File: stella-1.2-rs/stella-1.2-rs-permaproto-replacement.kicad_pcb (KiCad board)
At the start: 2 copper layers, 81.3 x 50.8 mm, 10 parts, among them J1 Conn_01x03, J2 Conn_01x04, U1 Triad, U2 Humidity, U3 Surface Temp, U4 Range

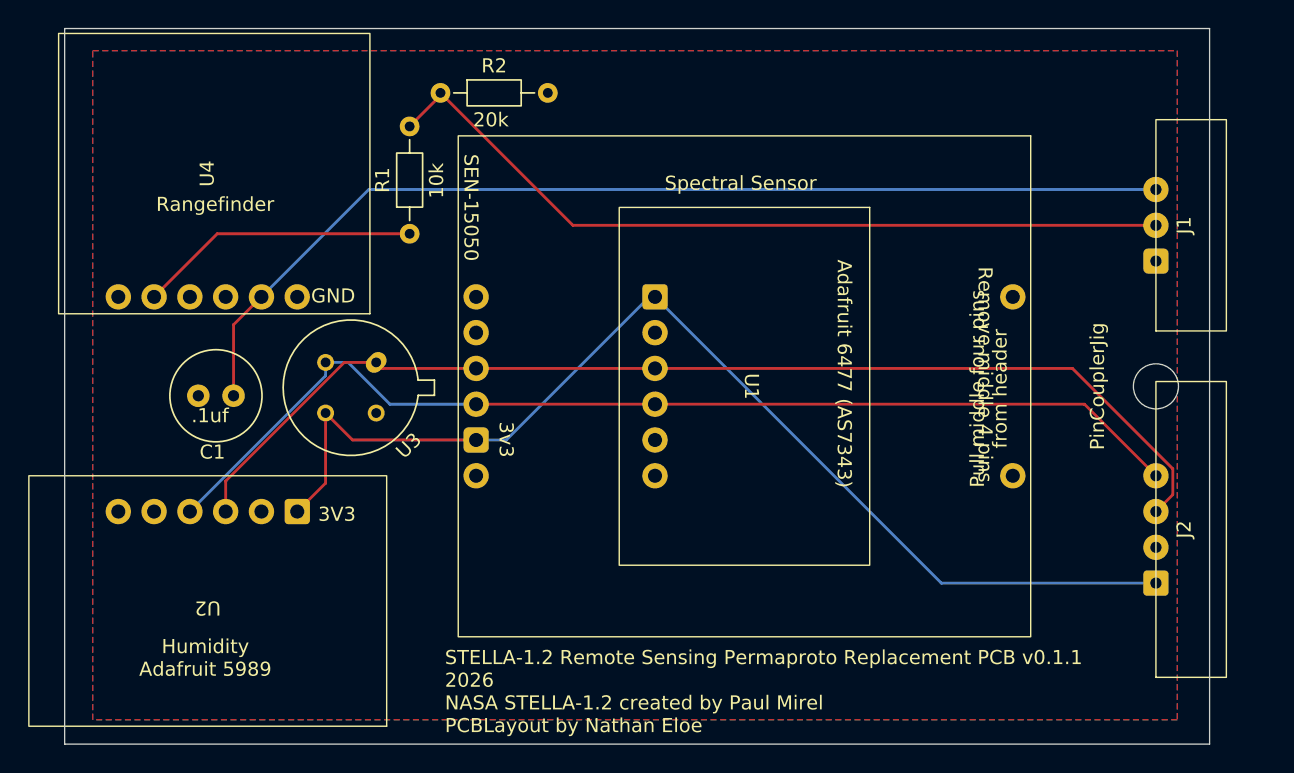
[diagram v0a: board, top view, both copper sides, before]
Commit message: Clean up silkscreen for RS PCB
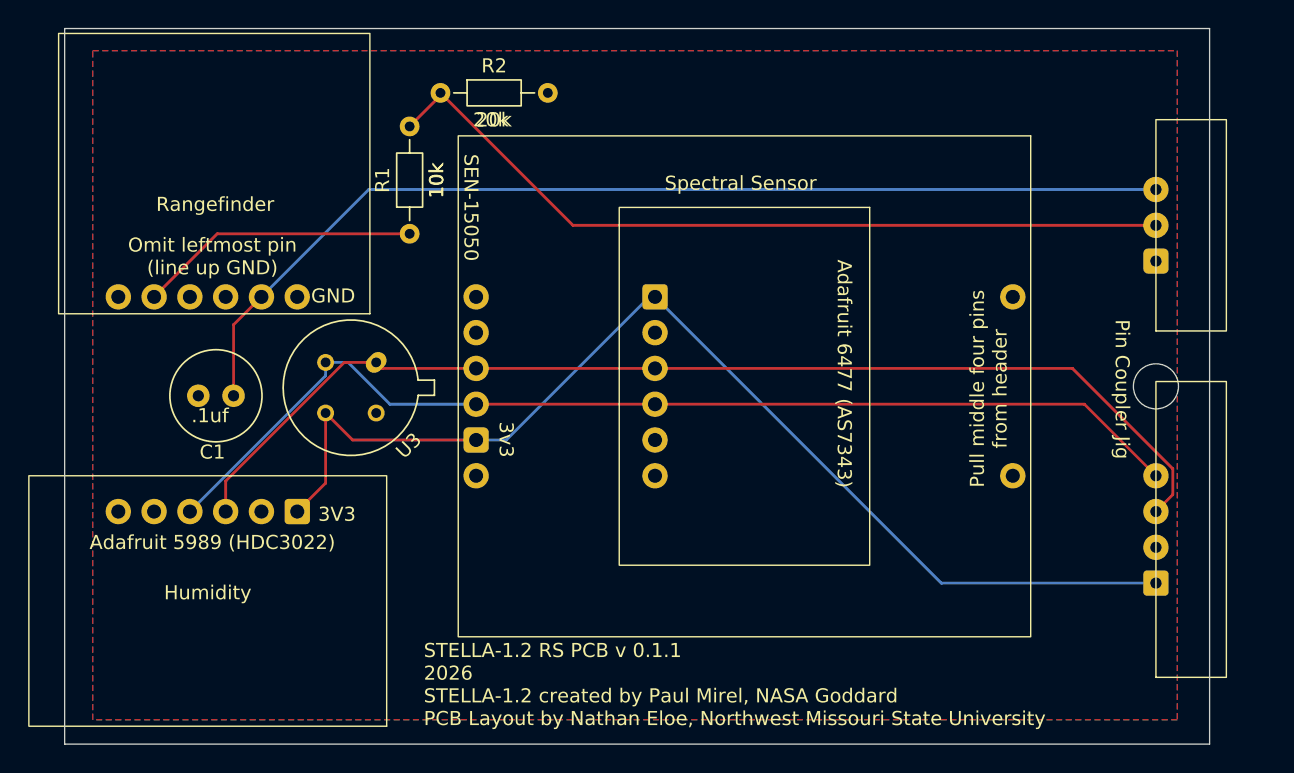
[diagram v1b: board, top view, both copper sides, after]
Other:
- board text added: "Adafruit 5989 (HDC3022)"
- board text added: "Humidity"
- board text added: "Omit leftmost pin (line up GND)"
- board text added: "Pin Coupler Jig"
- board text added: "STELLA-1.2 RS PCB v 0.1.1 2026 STELLA-1.2 created by Paul Mirel, NASA Goddard PCB Layout by Nathan Eloe, Northwest Missouri State University"
- board text removed: "Humidity Adafruit 5989"
- board text removed: "STELLA-1.2 Remote Sensing Permaproto Replacement PCB v0.1.1 2026 NASA STELLA-1.2 created by Paul Mirel PCBLayout by Nathan Eloe"
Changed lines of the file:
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@@
 			(unlocked yes)
 			(layer "F.SilkS")
+			(hide yes)
 			(effects
 				(font
@@
 			)
 		)
-		(fp_text user "Remove middle 4 pins"
-			(at -8.5 -16.5 270)
-			(unlocked yes)
-			(layer "F.SilkS")
-			(effects
-				(font
-					(size 1 1)
-					(thickness 0.1)
-				)
-				(justify left bottom)
-			)
-		)
 		(fp_text user "${REFERENCE}"
 			(at 0 2.5 270)
@@
 			(unlocked yes)
 			(layer "F.SilkS")
+			(hide yes)
 			(effects
 				(font
@@
 			(unlocked yes)
 			(layer "F.SilkS")
+			(hide yes)
 			(effects
 				(font
@@
 			(unlocked yes)
 			(layer "F.SilkS")
+			(hide yes)
 			(effects
 				(font
@@
 		(property "Value" "10k"
 			(at 3.81 1.92 90)
-			(layer "F.Fab")
+			(layer "F.SilkS")
 			(effects
 				(font
@@
 			(at 0 -4.15 90)
 			(layer "F.SilkS")
+			(hide yes)
 			(effects
 				(font
@@
 		(property "Value" "20k"
 			(at 3.81 1.92 0)
-			(layer "F.Fab")
+			(layer "F.SilkS")
 			(effects
 				(font
@@
 			(unlocked yes)
 			(layer "F.SilkS")
+			(hide yes)
 			(effects
 				(font
@@
 		)
 	)
-	(gr_text "STELLA-1.2 Remote Sensing Permaproto Replacement PCB v0.1.1\n2026\nNASA STELLA-1.2 created by Paul Mirel\nPCBLayout by Nathan Eloe\n"
-		(at 107 125 0)
-		(layer "F.SilkS")
-		(effects
-			(font
-				(size 1 1)
-				(thickness 0.1)
-			)
-			(justify left bottom)
-		)
-	)
 	(gr_text "20k"
 		(at 109 82 0)
@@
 		)
 	)
-	(gr_text "Humidity\nAdafruit 5989"
-		(at 90 121 0)
+	(gr_text "Humidity"
+		(at 90.17 115.57 0)
+		(layer "F.SilkS")
+		(effects
+			(font
+				(size 1 1)
+				(thickness 0.1)
+			)
+			(justify bottom)
+		)
+	)
+	(gr_text "Omit leftmost pin\n(line up GND)"
+		(at 90.5 92.5 0)
+		(layer "F.SilkS")
+		(effects
+			(font
+				(size 1 1)
+				(thickness 0.1)
+			)
+			(justify bottom)
+		)
+	)
+	(gr_text "Adafruit 5989 (HDC3022)"
+		(at 90.5 112 0)
 		(layer "F.SilkS")
 		(effects
@@
 		)
 	)
+	(gr_text "Pin Coupler Jig"
+		(at 154.5 100.54 270)
+		(layer "F.SilkS")
+		(effects
+			(font
+				(size 1 1)
+				(thickness 0.1)
+			)
+			(justify bottom)
+		)
+	)
+	(gr_text "STELLA-1.2 RS PCB v 0.1.1\n2026\nSTELLA-1.2 created by Paul Mirel, NASA Goddard\nPCB Layout by Nathan Eloe, Northwest Missouri State University"
+		(at 105.5 124.5 0)
+		(layer "F.SilkS")
+		(effects
+			(font
+				(size 1 1)
+				(thickness 0.15)
+			)
+			(justify left bottom)
+		)
+	)

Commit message: Tighten attribution to 3 lines
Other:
- board text added: "STELLA-1.2 RS PCB v 0.1.1, 2026 STELLA-1.2 created by Paul Mirel, NASA Goddard PCB Layout by Nathan Eloe, Northwest Missouri State University"
- board text added: "Surface Temp"
- board text removed: "STELLA-1.2 RS PCB v 0.1.1 2026 STELLA-1.2 created by Paul Mirel, NASA Goddard PCB Layout by Nathan Eloe, Northwest Missouri State University"
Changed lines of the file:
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@@
 		(tags "TO-39-4")
 		(property "Reference" "U3"
-			(at 0 -5.809999 225)
-			(layer "F.SilkS")
+			(at 0 -5.809999 45)
+			(layer "F.SilkS")
+			(hide yes)
 			(effects
 				(font
@@
 		)
 		(property "Value" "Surface Temp"
-			(at 0 5.809999 225)
+			(at 0 5.809999 45)
 			(layer "F.Fab")
 			(effects
@@
 		)
 		(property "Datasheet" ""
-			(at 0 0 225)
+			(at 0 0 45)
 			(layer "F.Fab")
 			(hide yes)
@@
 		)
 		(property "Description" ""
-			(at 0 0 225)
+			(at 0 0 45)
 			(layer "F.Fab")
 			(hide yes)
@@
 		)
 		(property "KiLib_Generator" "package/TO_SOT/THT"
-			(at 0 0 225)
+			(at 0 0 45)
 			(layer "F.SilkS")
 			(hide yes)
@@
 		)
 		(fp_text user "${REFERENCE}"
-			(at 0 -5.809999 225)
+			(at 0 -5.809999 45)
 			(layer "F.Fab")
 			(effects
@@
 		(layer "Edge.Cuts")
 	)
+	(gr_text "Surface Temp"
+		(at 100.5 101 0)
+		(layer "F.SilkS")
+		(effects
+			(font
+				(size 0.8 0.8)
+				(thickness 0.1)
+			)
+			(justify bottom)
+		)
+	)
 	(gr_text "Rangefinder"
 		(at 86.5 88 0)
@@
 		)
 	)
-	(gr_text "STELLA-1.2 RS PCB v 0.1.1\n2026\nSTELLA-1.2 created by Paul Mirel, NASA Goddard\nPCB Layout by Nathan Eloe, Northwest Missouri State University"
-		(at 105.5 124.5 0)
+	(gr_text "STELLA-1.2 RS PCB v 0.1.1, 2026\nSTELLA-1.2 created by Paul Mirel, NASA Goddard\nPCB Layout by Nathan Eloe, Northwest Missouri State University"
+		(at 105.5 123.5 0)
 		(layer "F.SilkS")
 		(effects

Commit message: Add pins for SHT4x to RS
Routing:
- net /I2C_SDA: track 76.9 -> 105.5 mm
- net /I2C_SCL: track 79.6 -> 105.7 mm
- net +3V3: track 80.2 -> 97.6 mm
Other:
- board text added: "Adafruit 4885/5776/6174 (SHT4X)"
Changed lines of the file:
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@@
+			(pintype "power_in")
+		)
+		(pad "1" thru_hole roundrect
+			(at 5.08 -6.35 180)
+			(size 1.8 1.8)
+			(drill 1)
+			(layers "*.Cu" "*.Mask")
+			(remove_unused_layers no)
+			(roundrect_rratio 0.15)
+			(net "+3V3")
+			(pinfunction "VCC_1")
 			(pintype "power_in")
 		)
@@
 			(pintype "power_in")
 		)
+		(pad "2" thru_hole circle
+			(at 0 -6.35 180)
+			(size 1.8 1.8)
+			(drill 1)
+			(layers "*.Cu" "*.Mask")
+			(remove_unused_layers no)
+			(net "GND")
+			(pinfunction "GND_2")
+			(pintype "power_in")
+		)
 		(pad "3" thru_hole circle
-			(at -1.27 6.35 180)
+			(at -2.54 -6.35 180)
 			(size 1.8 1.8)
 			(drill 1)
@@
 			(pintype "input")
 		)
+		(pad "3" thru_hole circle
+			(at -1.27 6.35 180)
+			(size 1.8 1.8)
+			(drill 1)
+			(layers "*.Cu" "*.Mask")
+			(remove_unused_layers no)
+			(net "/I2C_SCL")
+			(pinfunction "SCL_3")
+			(pintype "input")
+		)
 		(pad "4" thru_hole circle
-			(at 1.27 6.35 180)
+			(at -5.08 -6.35 180)
 			(size 1.8 1.8)
 			(drill 1)
@@
 			(pintype "output")
 		)
+		(pad "4" thru_hole circle
+			(at 1.27 6.35 180)
+			(size 1.8 1.8)
+			(drill 1)
+			(layers "*.Cu" "*.Mask")
+			(remove_unused_layers no)
+			(net "/I2C_SDA")
+			(pinfunction "SDA_4")
+			(pintype "output")
+		)
 		(pad "5" thru_hole circle
 			(at 3.81 6.35 180)
@@
 			(pinfunction "~{RES}_5")
 			(pintype "input+no_connect")
+		)
+		(pad "6" thru_hole circle
+			(at 2.54 -6.35 180)
+			(size 1.8 1.8)
+			(drill 1)
+			(layers "*.Cu" "*.Mask")
+			(remove_unused_layers no)
+			(net "unconnected-(U2-ALERT-Pad6)_1")
+			(pinfunction "ALERT_6")
+			(pintype "output+no_connect")
 		)
 		(pad "6" thru_hole circle
@@
 		)
 	)
+	(gr_text "3V3"
+		(at 80.5 122.5 0)
+		(layer "F.SilkS")
+		(effects
+			(font
+				(size 1 1)
+				(thickness 0.1)
+			)
+			(justify left bottom)
+		)
+	)
 	(gr_text "Rangefinder"
 		(at 86.5 88 0)
@@
 		)
 	)
+	(gr_text "3V3"
+		(at 120.5 93 0)
+		(layer "F.SilkS")
+		(effects
+			(font
+				(size 1 1)
+				(thickness 0.1)
+			)
+			(justify left bottom)
+		)
+	)
+	(gr_text "Adafruit 4885/5776/6174\n(SHT4X)"
+		(at 91 119.5 0)
+		(layer "F.SilkS")
+		(effects
+			(font
+				(size 1 1)
+				(thickness 0.1)
+			)
+		)
+	)
 	(gr_text "Humidity"
 		(at 90.17 115.57 0)
@@
 	)
 	(segment
+		(start 92.71 121.92)
+		(end 91.51 123.12)
+		(width 0.2)
+		(layer "F.Cu")
+		(net "/I2C_SCL")
+	)
+	(segment
 		(start 109.22 99.06)
 		(end 102.552102 99.06)
@@
 	)
 	(segment
+		(start 83.89 116.77)
+		(end 91.44 109.22)
+		(width 0.2)
+		(layer "F.Cu")
+		(net "/I2C_SCL")
+	)
+	(segment
 		(start 151.557057 99.06)
 		(end 121.92 99.06)
@@
 	)
 	(segment
+		(start 91.51 123.12)
+		(end 84.216418 123.12)
+		(width 0.2)
+		(layer "F.Cu")
+		(net "/I2C_SCL")
+	)
+	(segment
 		(start 102.552102 99.06)
 		(end 102.126051 98.633949)
@@
 	)
 	(segment
+		(start 83.89 122.793582)
+		(end 83.89 116.77)
+		(width 0.2)
+		(layer "F.Cu")
+		(net "/I2C_SCL")
+	)
+	(segment
 		(start 109.22 99.06)
 		(end 121.92 99.06)
@@
 	)
 	(segment
+		(start 84.216418 123.12)
+		(end 83.89 122.793582)
+		(width 0.2)
+		(layer "F.Cu")
+		(net "/I2C_SCL")
+	)
+	(segment
 		(start 157.48 106.68)
 		(end 152.4 101.6)
@@
 	)
 	(segment
+		(start 93.65 123.52)
+		(end 84.050732 123.52)
+		(width 0.2)
+		(layer "F.Cu")
+		(net "/I2C_SDA")
+	)
+	(segment
+		(start 95.25 121.92)
+		(end 93.65 123.52)
+		(width 0.2)
+		(layer "F.Cu")
+		(net "/I2C_SDA")
+	)
+	(segment
+		(start 84.050732 123.52)
+		(end 83.49 122.959267)
+		(width 0.2)
+		(layer "F.Cu")
+		(net "/I2C_SDA")
+	)
+	(segment
 		(start 152.4 101.6)
 		(end 121.92 101.6)
@@
 	)
 	(segment
+		(start 83.49 114.63)
+		(end 88.9 109.22)
+		(width 0.2)
+		(layer "F.Cu")
+		(net "/I2C_SDA")
+	)
+	(segment
+		(start 83.49 122.959267)
+		(end 83.49 114.63)
+		(width 0.2)
+		(layer "F.Cu")
+		(net "/I2C_SDA")
+	)
+	(segment
 		(start 109.22 101.6)
 		(end 121.92 101.6)
@@
 		(width 0.2)
 		(layer "F.Cu")
+		(net "+3V3")
+	)
+	(segment
+		(start 85.09 120.65)
+		(end 96.52 109.22)
+		(width 0.2)
+		(layer "F.Cu")
+		(net "+3V3")
+	)
+	(segment
+		(start 85.09 121.92)
+		(end 85.09 120.65)
+		(width 0.2)
+		(layer "F.Cu")
